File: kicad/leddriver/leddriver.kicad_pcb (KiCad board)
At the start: 2 copper layers, 37.8 x 19.3 mm, 7 parts, among them J1 Conn_01x02_Male, J2 Conn_01x01_Male, U1 TLC555xP

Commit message: Add new code
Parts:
- added BZ1: Buzzer, Buzzer_Beeper:MagneticBuzzer_ProSignal_ABI-010-RC, F.Cu at (165.9, 99.6)
- added C3: 4.7uF, Capacitor_THT:C_Disc_D4.3mm_W1.9mm_P5.00mm, F.Cu at (174.5, 90.2)
- added C4: .01uF, Capacitor_THT:C_Disc_D4.3mm_W1.9mm_P5.00mm, F.Cu at (159.0, 90.2)
- added J3: Conn_01x01_Male, Connector_PinHeader_2.54mm:PinHeader_1x01_P2.54mm_Vertical, F.Cu at (144.5, 73.4)
- added Q1: 2N3904, leddriver:TO-92_HandSolder_Large_Pad, F.Cu at (152.7, 99.1)
- added R3: 68k, Resistor_THT:R_Axial_DIN0204_L3.6mm_D1.6mm_P2.54mm_Vertical, F.Cu at (126.7, 84.6)
- added R4: 1k, Resistor_THT:R_Axial_DIN0204_L3.6mm_D1.6mm_P2.54mm_Vertical, F.Cu at (168.4, 77.2)
- added R5: 68k, Resistor_THT:R_Axial_DIN0204_L3.6mm_D1.6mm_P2.54mm_Vertical, F.Cu at (168.4, 83.3)
- added SW1: SW_Push, Button_Switch_THT:SW_PUSH_6mm_H5mm, F.Cu at (124.7, 90.7)
- added U2: TLC555xP, Package_DIP:DIP-8_W7.62mm, F.Cu at (154.2, 77.2)
- C1: value 0.01uF -> 1uF; footprint Capacitor_SMD:C_1206_3216Metric_Pad1.33x1.80mm_HandSolder -> Capacitor_THT:C_Disc_D4.3mm_W1.9mm_P5.00mm
- C2: value 10uF -> .01uF; footprint Capacitor_SMD:C_1206_3216Metric_Pad1.33x1.80mm_HandSolder -> Capacitor_THT:C_Disc_D4.3mm_W1.9mm_P5.00mm
- J1: value Conn_01x02_Male -> Conn_01x01_Male; footprint Connector_PinSocket_2.54mm:PinSocket_1x02_P2.54mm_Vertical -> Connector_PinHeader_2.54mm:PinHeader_1x01_P2.54mm_Vertical
- J2: value Conn_01x01_Male -> Conn_01x02_Male; footprint Connector_PinHeader_2.54mm:PinHeader_1x01_P2.54mm_Vertical -> Connector_PinSocket_2.54mm:PinSocket_1x02_P2.54mm_Vertical
- R1, R2: footprint Resistor_SMD:R_0805_2012Metric_Pad1.20x1.40mm_HandSolder -> Resistor_THT:R_Axial_DIN0204_L3.6mm_D1.6mm_P2.54mm_Vertical
- moved J2 47.1 mm to (175.3, 76.7)
- moved R1 24.8 mm to (136.9, 95.5), turned to 0 degrees
- moved C2 24.5 mm to (126.0, 73.9), turned to 270 degrees
- moved C1 14.1 mm to (141.3, 89.9)
- moved R2 13.1 mm to (137.4, 73.4), turned to 180 degrees
- moved J1 12.0 mm to (147.8, 80.0), turned to 0 degrees
- moved U1 9.20 mm to (140.0, 85.3), turned to 180 degrees
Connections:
- J1 pad 1: GND -> OUT
- J2 pad 1: Net-(J2-Pad1) -> VCC
- R1 pad 2: Net-(R1-Pad2) -> Net-(C1-Pad1)
- R2 pad 1: Net-(R1-Pad2) -> VCC
- R2 pad 2: Net-(C2-Pad1) -> Net-(R2-Pad2)
- U1 pad 2: Net-(C2-Pad1) -> Net-(R2-Pad2)
- U1 pad 3: Net-(J2-Pad1) -> OUT1
- U1 pad 5: Net-(C1-Pad1) -> Net-(C2-Pad1)
- U1 pad 6: Net-(C2-Pad1) -> Net-(R2-Pad2)
- U1 pad 7: Net-(R1-Pad2) -> (no net)
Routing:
- net VCC: track 52.3 -> 122.5 mm
- net Net-(R2-Pad2): track 0.00 -> 35.5 mm
- net OUT: track 0.00 -> 23.4 mm
- net Net-(C1-Pad1): track 9.65 -> 28.3 mm
- net Net-(BZ1-Pad1): track 0.00 -> 18.1 mm
- net OUT1: track 0.00 -> 16.1 mm
- net Net-(C3-Pad1): track 0.00 -> 16.0 mm
- net Net-(R4-Pad2): track 0.00 -> 10.2 mm
- net Net-(R1-Pad2): track 9.60 -> 0.00 mm
- net GND: track 0.00 -> 8.24 mm
- net Net-(J2-Pad1): track 7.11 -> 0.00 mm
- net Net-(C4-Pad1): track 0.00 -> 6.49 mm
- net Net-(C2-Pad1): track 9.45 -> 7.93 mm
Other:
- board size 37.8 x 19.3 mm -> 60.5 x 39.9 mm
- board text added: "Bike Indicator v1.0"

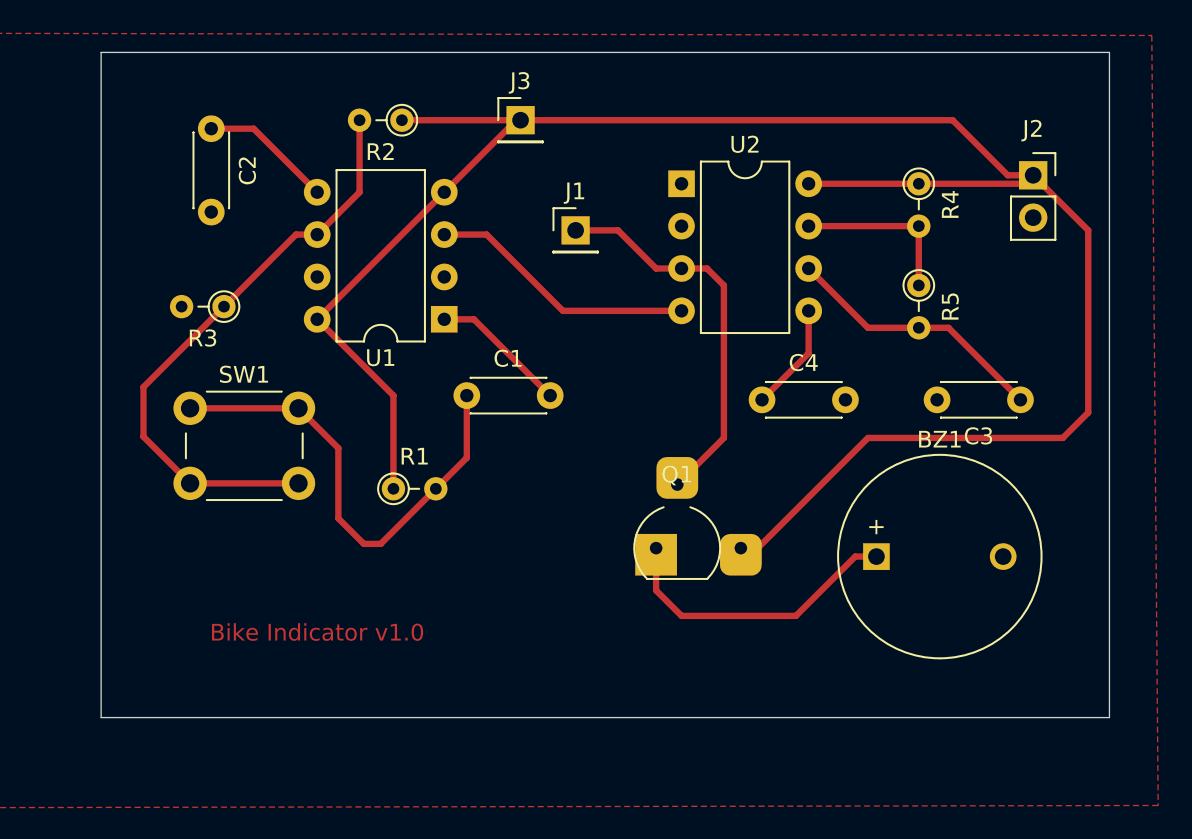
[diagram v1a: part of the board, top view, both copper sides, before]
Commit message: Add new led driver schematic
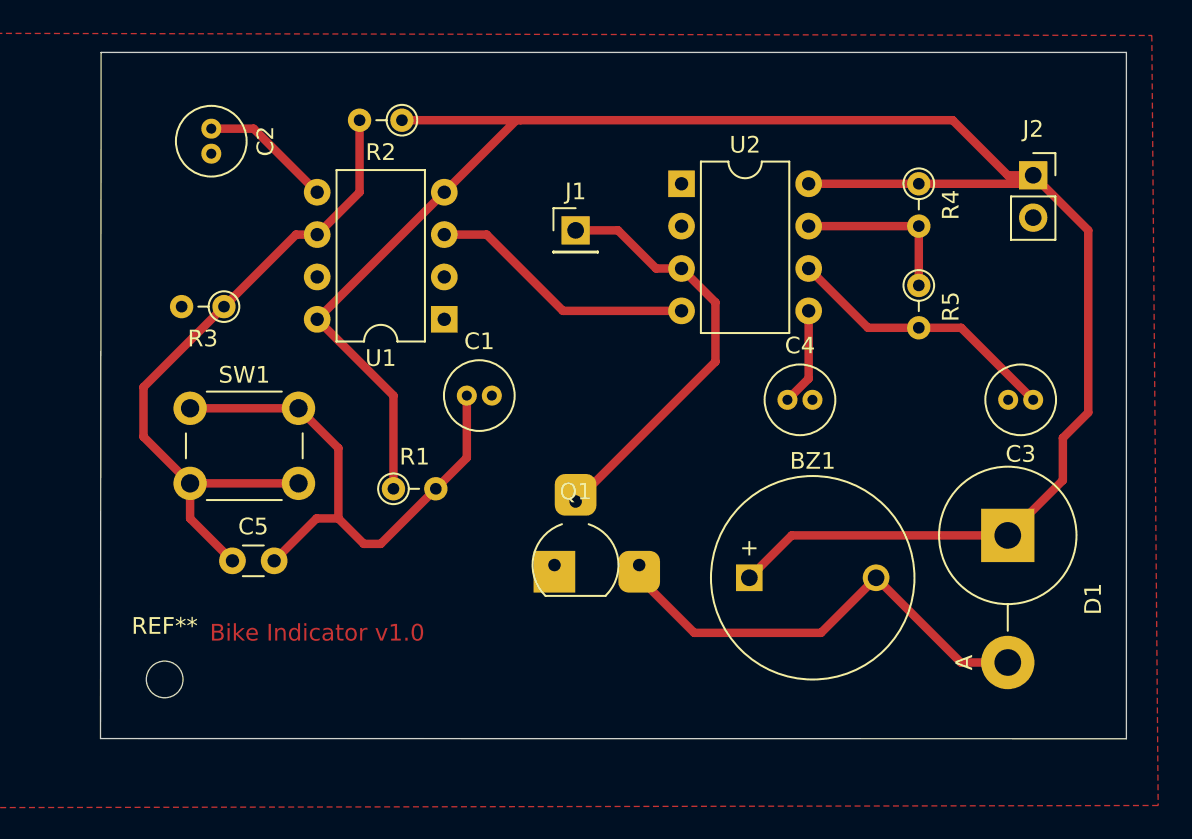
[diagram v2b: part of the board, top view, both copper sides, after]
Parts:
- removed J3: Conn_01x01_Male, Connector_PinHeader_2.54mm:PinHeader_1x01_P2.54mm_Vertical
- added C5: 22pf, Capacitor_THT:C_Disc_D3.0mm_W1.6mm_P2.50mm, F.Cu at (127.3, 99.8)
- added D1: D, Diode_THT:D_5KPW_P7.62mm_Vertical_AnodeUp, F.Cu at (173.7, 98.3)
- added REF**: MountingHole_2.2mm_M2, MountingHole:MountingHole_2.2mm_M2, F.Cu at (123.2, 106.9)
- C1, C2, C3, C4: footprint Capacitor_THT:C_Disc_D4.3mm_W1.9mm_P5.00mm -> Capacitor_THT:C_Radial_D4.0mm_H5.0mm_P1.50mm
- moved BZ1 7.73 mm to (158.2, 100.8)
- moved Q1 6.18 mm to (146.6, 100.1)
- moved C4 1.52 mm to (160.5, 90.2)
- moved C3 0.76 mm to (175.3, 90.2)
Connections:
- net Net-(C2-Pad1) renamed /CTRL1
- net Net-(C3-Pad1) renamed /THR2
- net Net-(C4-Pad1) renamed /CTRL2
- net Net-(R2-Pad2) renamed /THR1
- net Net-(R4-Pad2) renamed /DIS2
- BZ1 pad 1: Net-(BZ1-Pad1) -> VCC
- BZ1 pad 2: GND -> Net-(BZ1-Pad2)
- Q1 pad 1: Net-(BZ1-Pad1) -> GND
- Q1 pad 3: VCC -> Net-(BZ1-Pad2)
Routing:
- net Net-(BZ1-Pad2): track 0.00 -> 27.7 mm
- net Net-(BZ1-Pad1): track 18.1 -> 0.00 mm
- net GND: track 8.24 -> 0.00 mm
- net /THR1: track 35.5 -> 41.2 mm
- net Net-(C1-Pad1): track 28.3 -> 33.2 mm
- net OUT: track 23.4 -> 25.6 mm
- net VCC: track 122.5 -> 123.6 mm
- net /THR2: track 16.0 -> 16.7 mm
- net /CTRL2: track 6.49 -> 5.86 mm
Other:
- board size 60.5 x 39.9 mm -> 61.5 x 41.1 mm
- net class homemade added: clearance 0.508, trace_width 0.508, via_dia 0.8, via_drill 0.4

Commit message: Add change according to 12v test
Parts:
- removed REF**: MountingHole_2.2mm_M2, MountingHole:MountingHole_2.2mm_M2
- added R6: 10k, Resistor_THT:R_Axial_DIN0204_L3.6mm_D1.6mm_P2.54mm_Vertical, F.Cu at (148.5, 90.2)
- added R7: 10k, Resistor_THT:R_Axial_DIN0204_L3.6mm_D1.6mm_P2.54mm_Vertical, F.Cu at (156.0, 94.0)
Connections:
- Q1 pad 2: OUT -> Net-(Q1-Pad2)
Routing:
- net Net-(Q1-Pad2): track 0.00 -> 14.7 mm
- net GND: track 0.00 -> 7.64 mm
- net OUT: track 25.6 -> 19.9 mm

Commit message: improve the current consumption at standby
20mA to 10mA  now
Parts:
- removed C5: 22pf, Capacitor_THT:C_Disc_D3.0mm_W1.6mm_P2.50mm
- R4: value 1k -> 68k
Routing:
- net /THR1: track 41.2 -> 35.5 mm
- net Net-(C1-Pad1): track 33.2 -> 28.3 mm

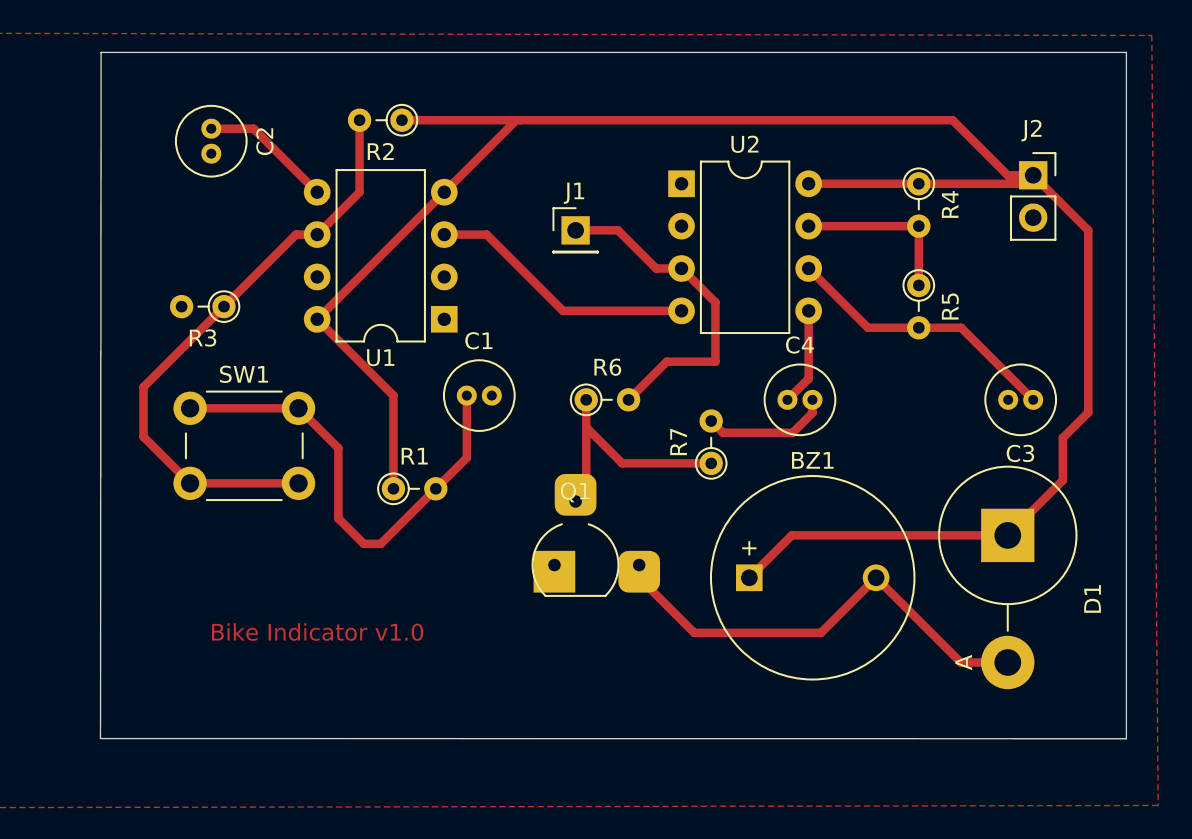
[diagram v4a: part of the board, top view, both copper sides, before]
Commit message: update according to new findings on breadboard.
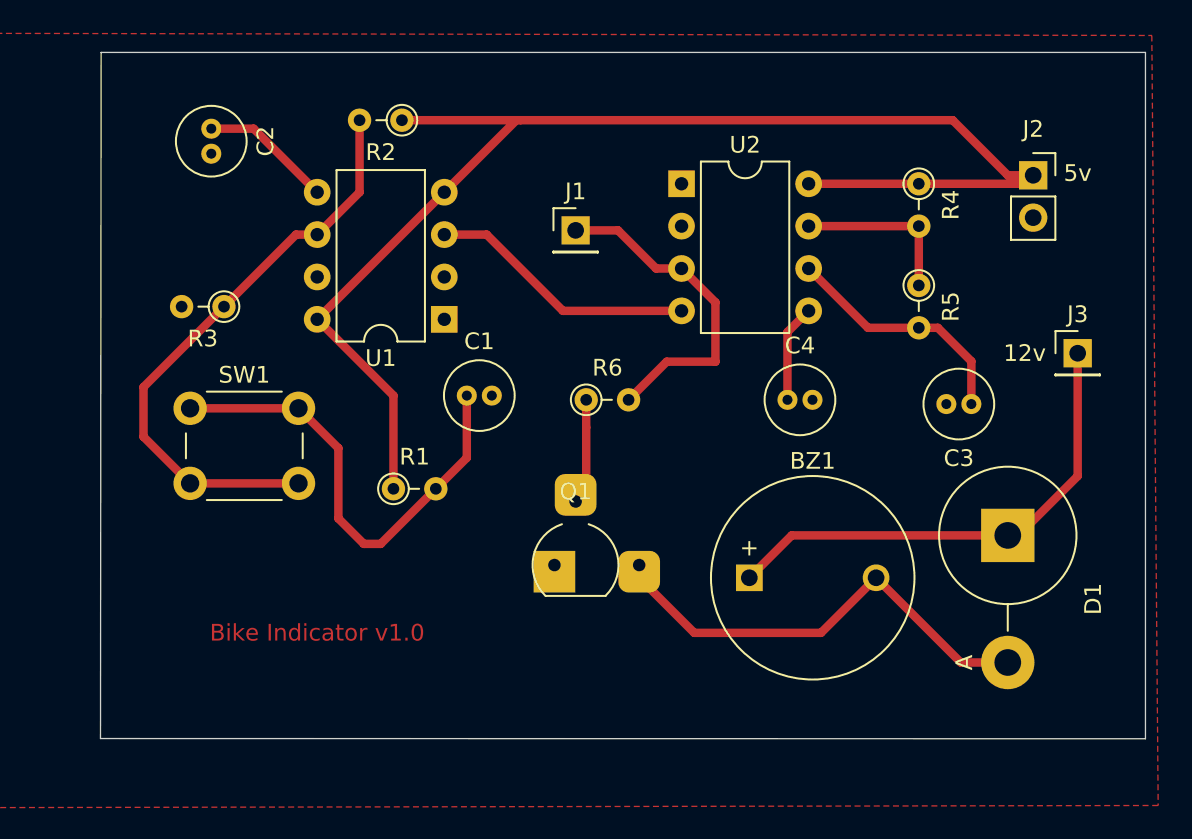
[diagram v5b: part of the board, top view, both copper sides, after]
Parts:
- removed R7: 10k, Resistor_THT:R_Axial_DIN0204_L3.6mm_D1.6mm_P2.54mm_Vertical
- added J3: Conn_01x01_Male, Connector_PinHeader_2.54mm:PinHeader_1x01_P2.54mm_Vertical, F.Cu at (177.9, 87.4)
- R6: value 10k -> 1k
- moved C3 3.72 mm to (171.6, 90.4)
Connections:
- BZ1 pad 1: VCC -> VCCQ
- D1 pad 1: VCC -> VCCQ
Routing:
- net VCC: track 123.6 -> 82.1 mm
- net VCCQ: track 0.00 -> 29.6 mm
- net Net-(Q1-Pad2): track 14.7 -> 6.36 mm
- net GND: track 7.64 -> 0.00 mm
- net /THR2: track 16.7 -> 14.6 mm
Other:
- board size 61.5 x 41.1 mm -> 62.6 x 41.1 mm
- board text added: "12v"
- board text added: "5v"

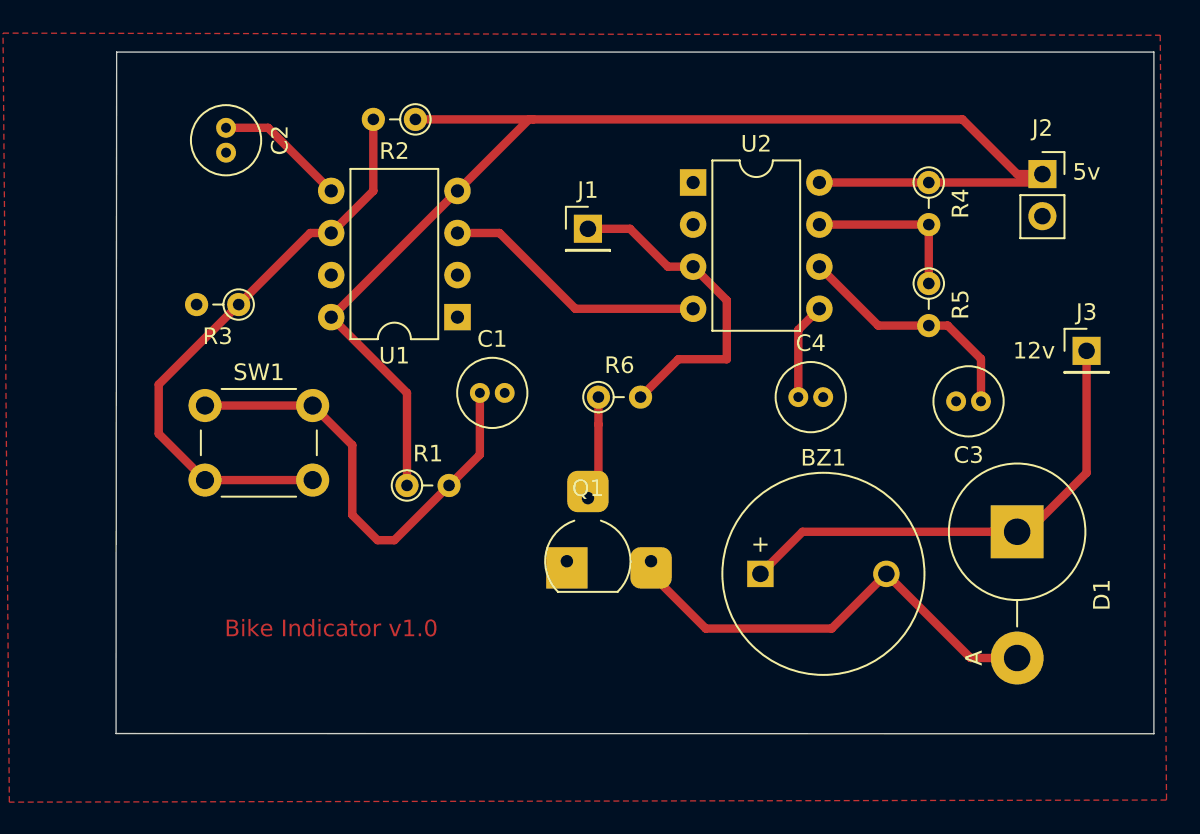
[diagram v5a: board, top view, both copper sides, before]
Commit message: chnage the schematic
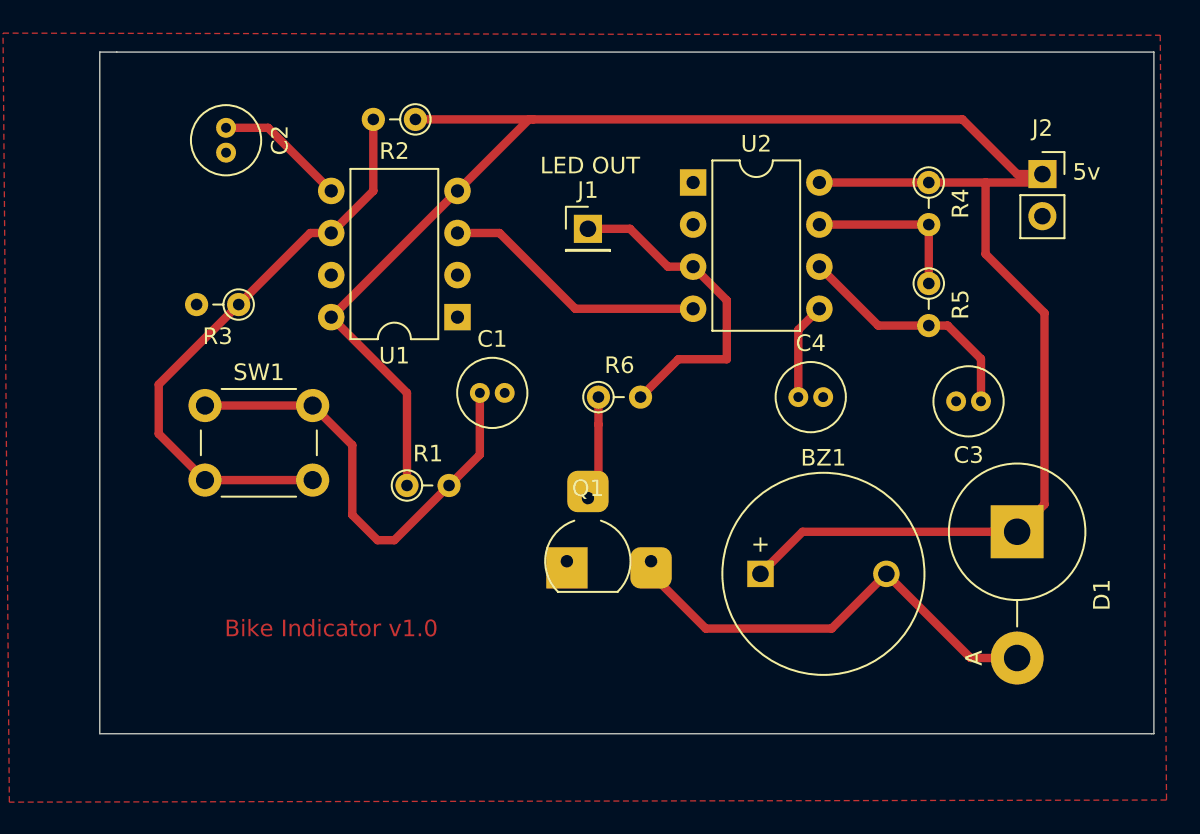
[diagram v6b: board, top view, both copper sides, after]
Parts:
- removed J3: Conn_01x01_Male, Connector_PinHeader_2.54mm:PinHeader_1x01_P2.54mm_Vertical
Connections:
- BZ1 pad 1: VCCQ -> VCC
- D1 pad 1: VCCQ -> VCC
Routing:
- net VCC: track 82.1 -> 122.5 mm
- net VCCQ: track 29.6 -> 0.00 mm
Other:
- board size 62.6 x 41.1 mm -> 63.6 x 41.1 mm
- board text added: "LED OUT"
- board text removed: "12v"
